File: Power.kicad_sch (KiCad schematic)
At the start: 60 parts, among them IC701 TPS63021DSJR, Q701 IRLML6402, U702 TLV9304IDR

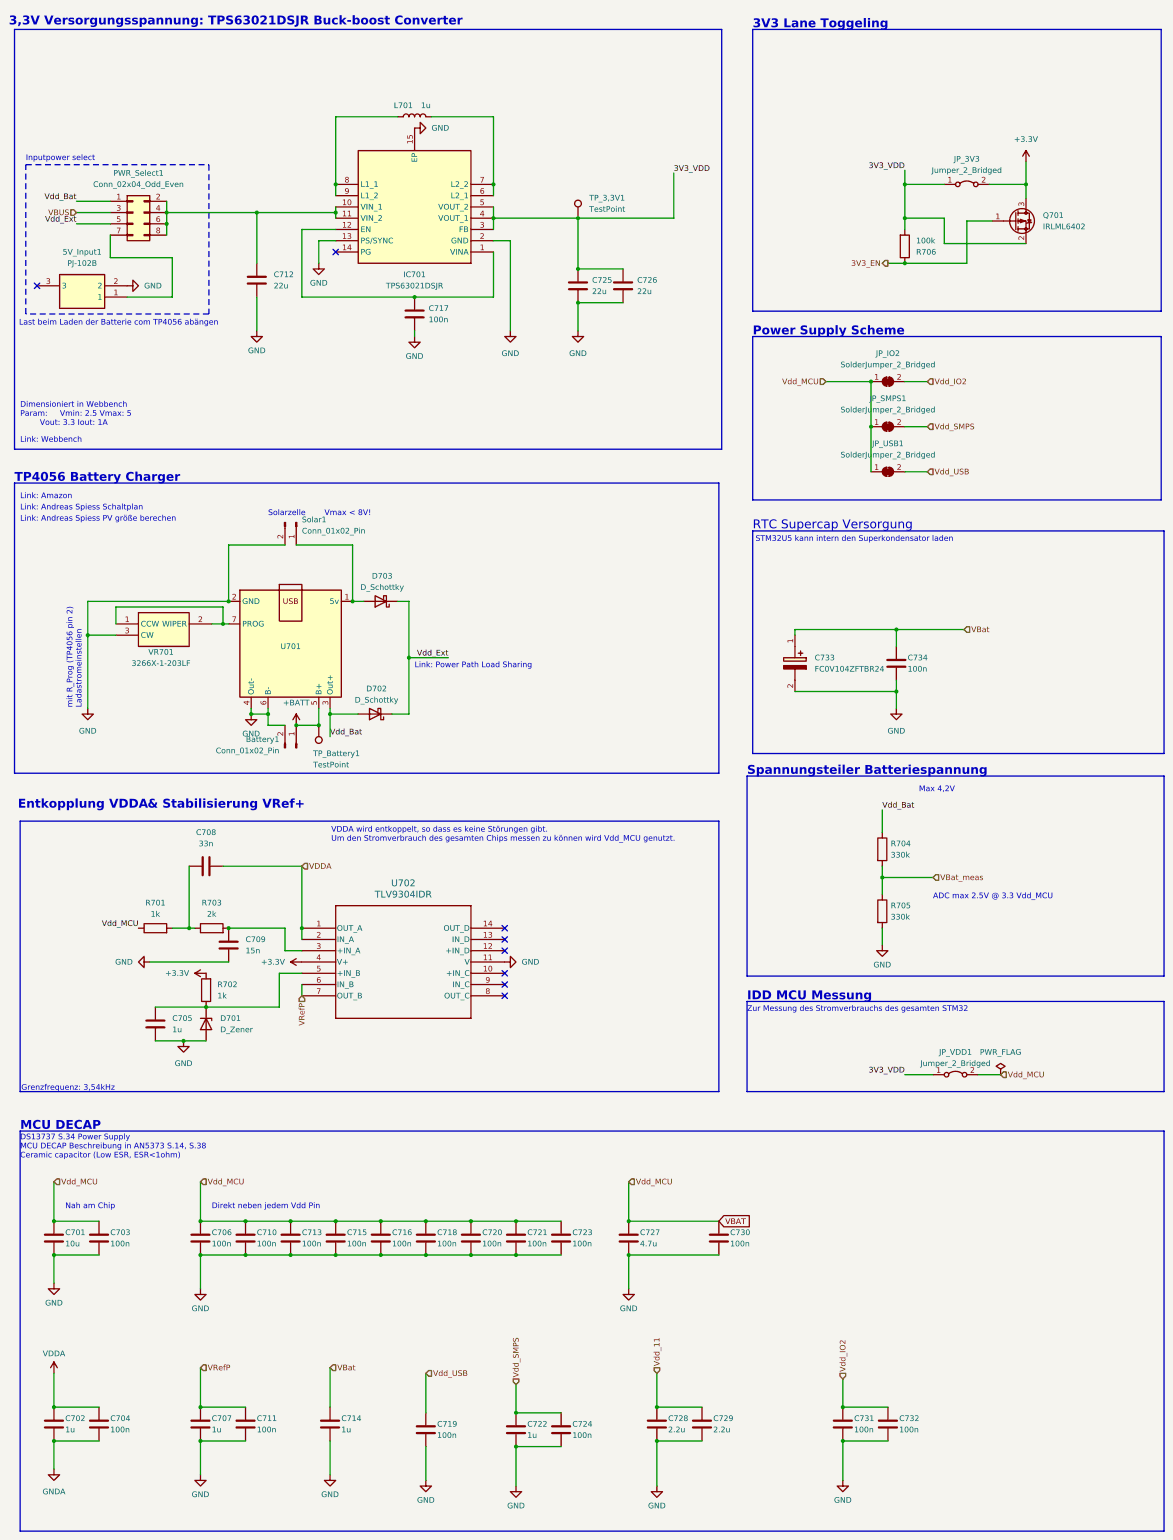
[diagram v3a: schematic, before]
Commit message: new layout
- recreation of the layout
- changed connection of ADC to MCU
- cleaner layout
- battery (supercap) for rtc
- crystal nearby the mcu
- 3V3 layer can be switched on/off separated from the mcu
- diode replaced with MOSFET
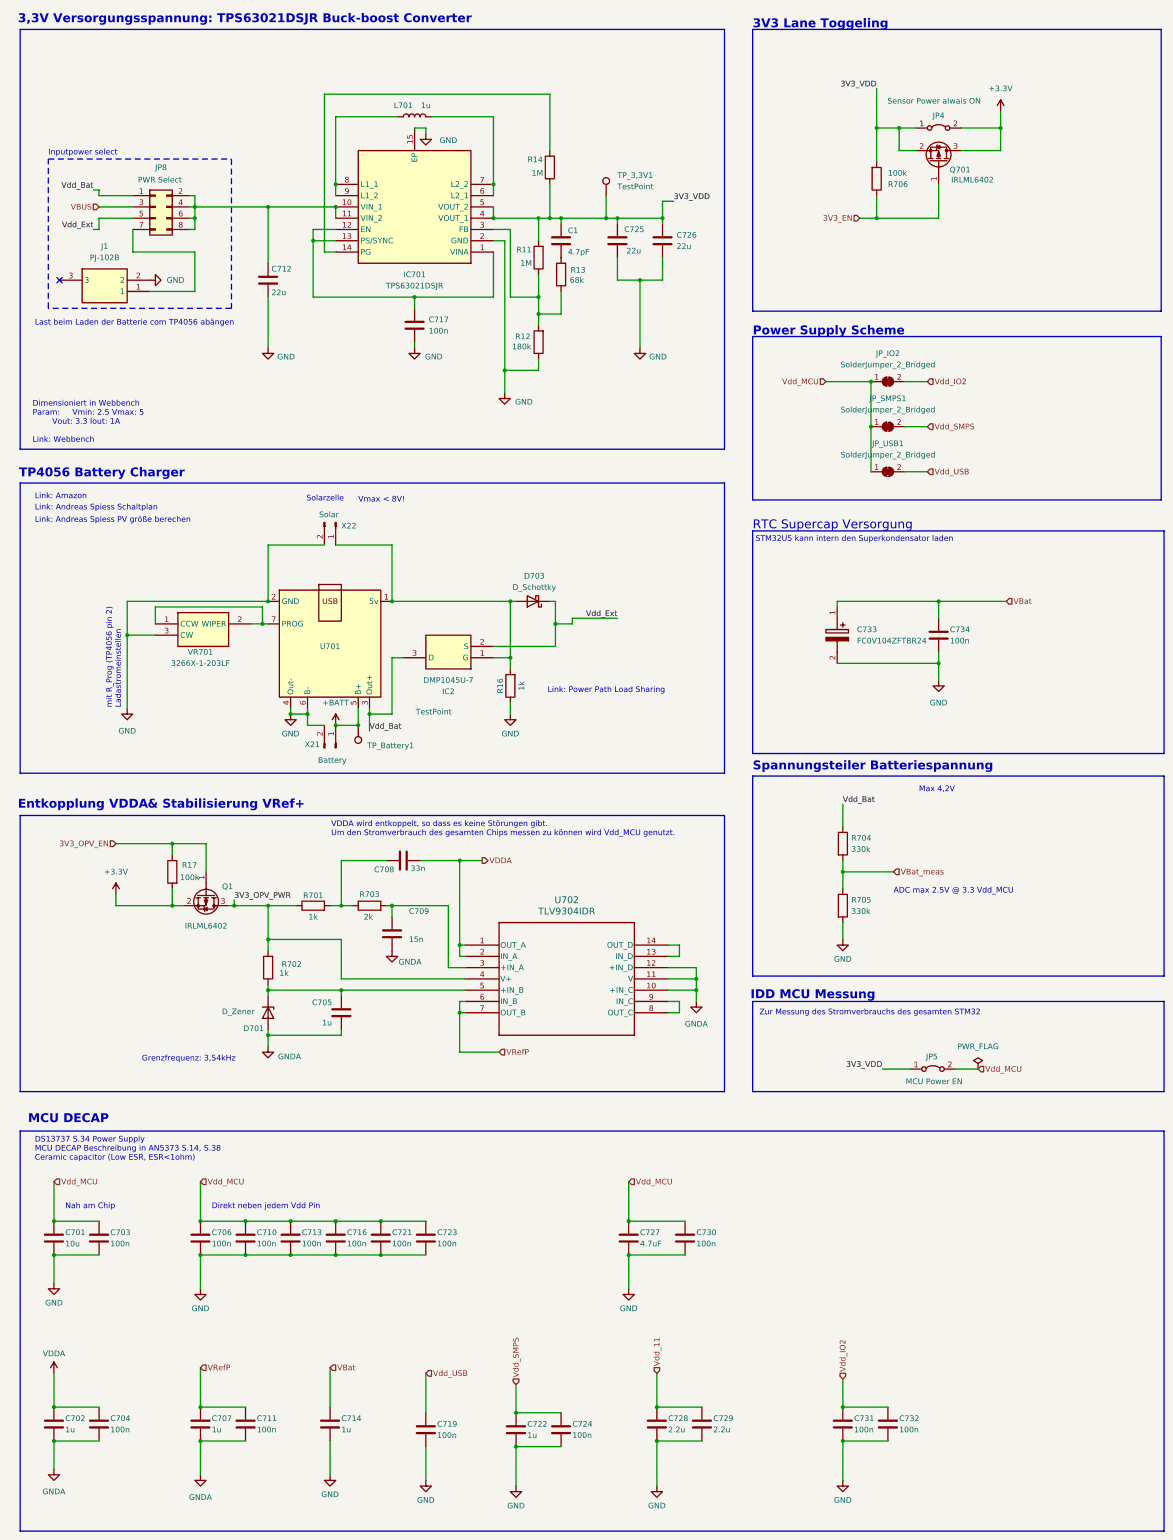
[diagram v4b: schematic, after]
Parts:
- removed C715, C718, C720: 100n, Capacitor_SMD:C_0805_2012Metric_Pad1.18x1.45mm_HandSolder, symbol Device:C
- removed D702: D_Schottky, Diode_SMD:D_SOD-123F, symbol Device:D_Schottky
- added C1: 4.7pF, Capacitor_SMD:C_0805_2012Metric_Pad1.18x1.45mm_HandSolder, symbol Device:C
- added IC2: DMP1045U-7, Bibliothek:SOT50P160X90-3N, symbol Transistor_FET:DMP1045U-7
- added Q1: IRLML6402, Package_TO_SOT_SMD:SOT-23, symbol Transistor_FET:IRLML6402
- added R11, R14: 1M, Resistor_SMD:R_0805_2012Metric_Pad1.20x1.40mm_HandSolder, symbol Device:R
- added R12: 180k, Resistor_SMD:R_0805_2012Metric_Pad1.20x1.40mm_HandSolder, symbol Device:R
- added R13: 68k, Resistor_SMD:R_0805_2012Metric_Pad1.20x1.40mm_HandSolder, symbol Device:R
- added R16: 1k, Resistor_SMD:R_0805_2012Metric_Pad1.20x1.40mm_HandSolder, symbol Device:R
- added R17: 100k, Resistor_SMD:R_0805_2012Metric_Pad1.20x1.40mm_HandSolder, symbol Device:R
- C708: Mouser Part Number 80-C0805C153K1R -> 710-885012207095
- C709: Mouser Part Number 80-C0805C153K1R -> 80-C0805C153K1R
- C727: value 4.7u -> 4.7uF
- C733: footprint CAPAE1080X550N -> Bibliothek:CAPAE1080X550N
- J1: renamed from 5V_Input1; footprint PJ-102B:PJ102B -> Connector_BarrelJack:BarrelJack_CUI_PJ-102AH_Horizontal
- JP4: renamed from JP_3V3; Mouser Part Number (none) -> 523-G800NA306018EU
- JP5: renamed from JP_VDD1; Mouser Part Number (none) -> 523-G800NA306018EU
- JP8: renamed from PWR_Select1; Mouser Part Number (none) -> 649-1012938190403BLF
- JP_IO2, JP_SMPS1, JP_USB1, TP_3,3V1, TP_Battery1, U701: now left out of the parts list
- L701: Mouser Part Number 815-ASMCI-0805-1R0MT -> 80-C0805C105K3RACTM
- Q701: Mouser Part Number (none) -> 942-IRLML6402TRPBF
- U702: Mouser Part Number (none) -> 595-TLV9304IDR
- renumbered Battery1 to X21, Solar1 to X22
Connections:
- net +3.3V: now also Q1.2 (S), R17.2; no longer R702.2, U702.4 (V+)
- net 3V3_VDD: now also C1.1, R11.2, R14.1; no longer IC701.3 (FB)
- net GND: now also R12.1, R16.1; no longer C705.2, C707.2, C709.2, C711.2, D701.2 (A), IC701.13 (PS/SYNC), U702.11 (V)
- net GNDA: now also C705.2, C707.2, C709.2, C711.2, D701.2 (A), U702.10 (+IN_C), U702.11 (V), U702.12 (+IN_D)
- net Vdd_Bat: now also IC2.3 (D)
- net Vdd_Ext: now also IC2.2 (S)
- net at D703.2 (A), U701.1 (5v), X22.1 (Pin_1): now also IC2.1 (G), R16.2
- net at U702.13 (IN_D): now also U702.14 (OUT_D)
- net at U702.8 (OUT_C): now also U702.9 (IN_C)
- net at C717.1, IC701.1 (VINA), IC701.12 (EN): now also IC701.13 (PS/SYNC)
- net at IC701.14 (PG): now also R14.2
- net VBAT renamed Vdd_MCU
- net Vdd_MCU: no longer R701.1
- new net: C1.2, R13.2
- new net: IC701.3 (FB), R11.1, R12.2, R13.1
- new net 3V3_OPV_EN: Q1.1 (G), R17.1
- new net 3V3_OPV_PWR: Q1.3 (D), R701.1, R702.2, U702.4 (V+)
- no-connect marks 8 -> 1
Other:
- moved on the sheet: C705, C708, C709, C712, C716, C717, C721, C723, C725, C726, C730, C733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
